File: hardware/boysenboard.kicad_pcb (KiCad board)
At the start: 4 copper layers, 68.6 x 53.3 mm, 97 parts, among them J1 1050171001, J2 54-00164, J3 NPTC101KFXC-RC, J4 NPTC081KFXC-RC, J5 Micro-SD, J6 NPTC081KFXC-RC, J7 NPTC061KFXC-RC, Q1 BSS308PEH6327XTSA1, SW1 PTS645SL70SMTR92LFS, U1 F1C200s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

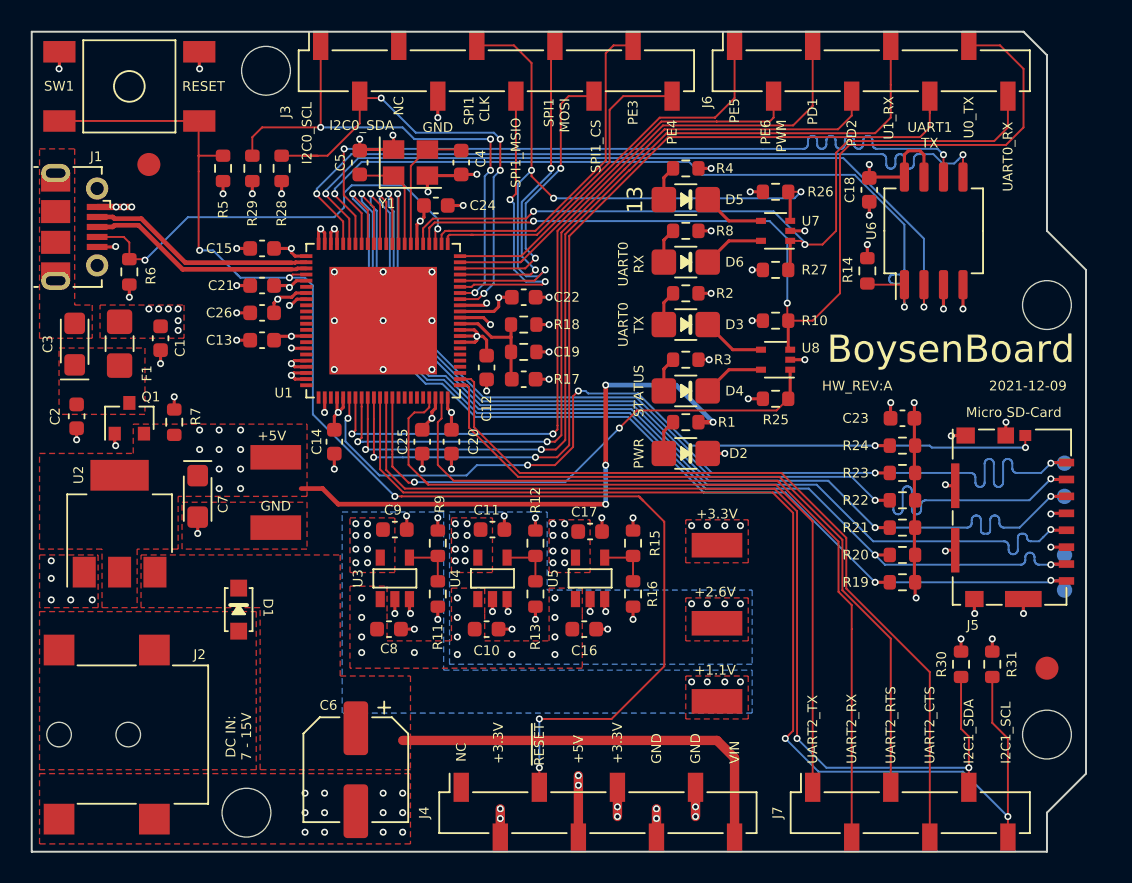
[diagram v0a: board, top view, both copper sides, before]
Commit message: Fixed footprint references and kicad 5->6 models
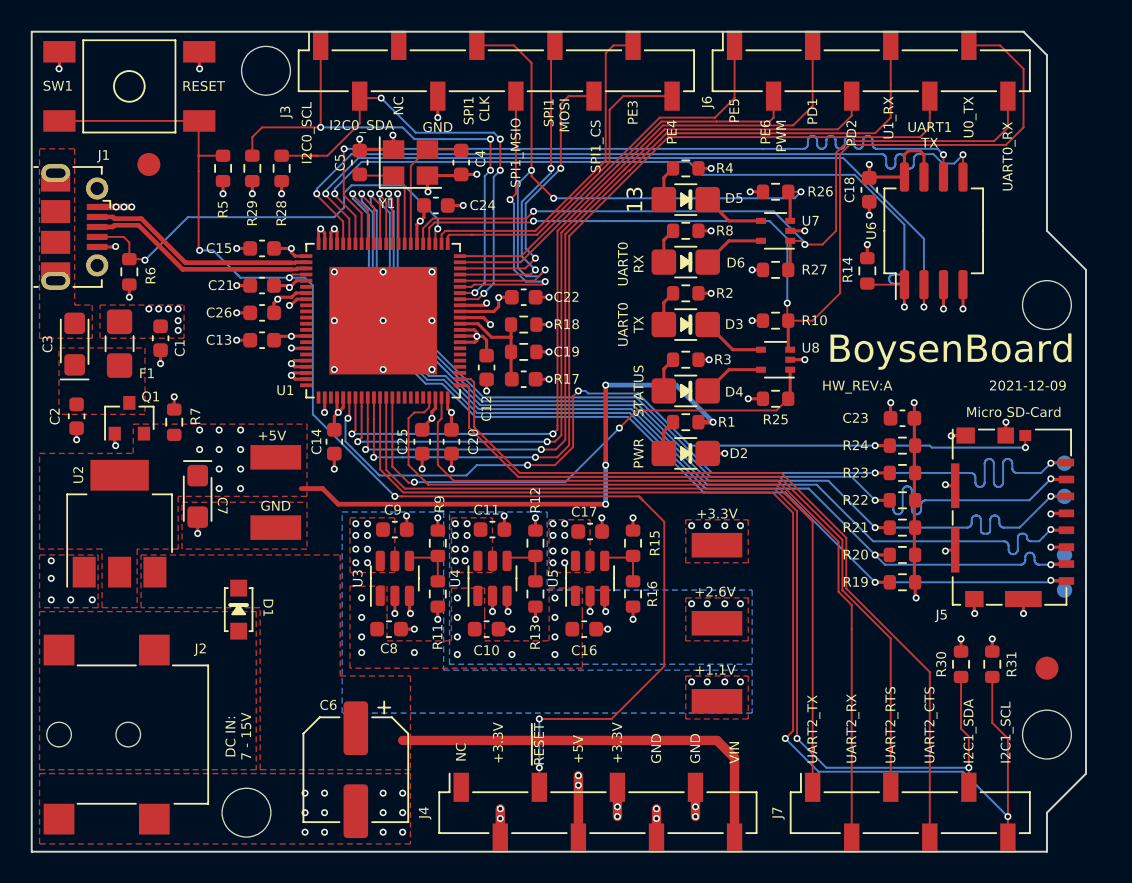
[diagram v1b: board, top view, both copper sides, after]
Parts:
- C3, C7: footprint licheeduino:CP_EIA-3216-18_Kemet-A -> boysenboard:CP_EIA-3216-18_Kemet-A
- D1: footprint licheeduino:D_SOD-123F -> boysenboard:D_SOD-123F
- D2, D3, D4, D5, D6: footprint licheeduino:LED_1206_3216Metric_Castellated -> boysenboard:LED_1206_3216Metric_Castellated
- F1: footprint licheeduino:Fuse_1206_3216Metric_Castellated -> boysenboard:Fuse_1206_3216Metric_Castellated
- H1, H2, H3, H4: footprint licheeduino:mounting_hole_125mil -> boysenboard:mounting_hole_125mil
- J1: footprint licheeduino:USB_Micro-B_Molex-105017-0001 -> boysenboard:USB_Micro-B_Molex-105017-0001
- J2: footprint licheeduino:barrel_jack_2.1mm -> boysenboard:barrel_jack_2.1mm
- J5: footprint licheeduino:micro-sd -> boysenboard:micro-sd
- SW1: footprint licheeduino:switch_tactile_6x6mm_smt -> boysenboard:switch_tactile_6x6mm_smt
- TP1, TP2, TP3, TP4, TP5: footprint licheeduino:test_point_RCSCTE -> boysenboard:test_point_RCSCTE
- U1: footprint licheeduino:QFN-88 -> boysenboard:QFN-88
- U3, U4, U5: footprint licheeduino:SOT-25 -> Package_TO_SOT_SMD:SOT-23-6

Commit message: Fixed PCB DRC violations caused by Kicad 5->6 conversion
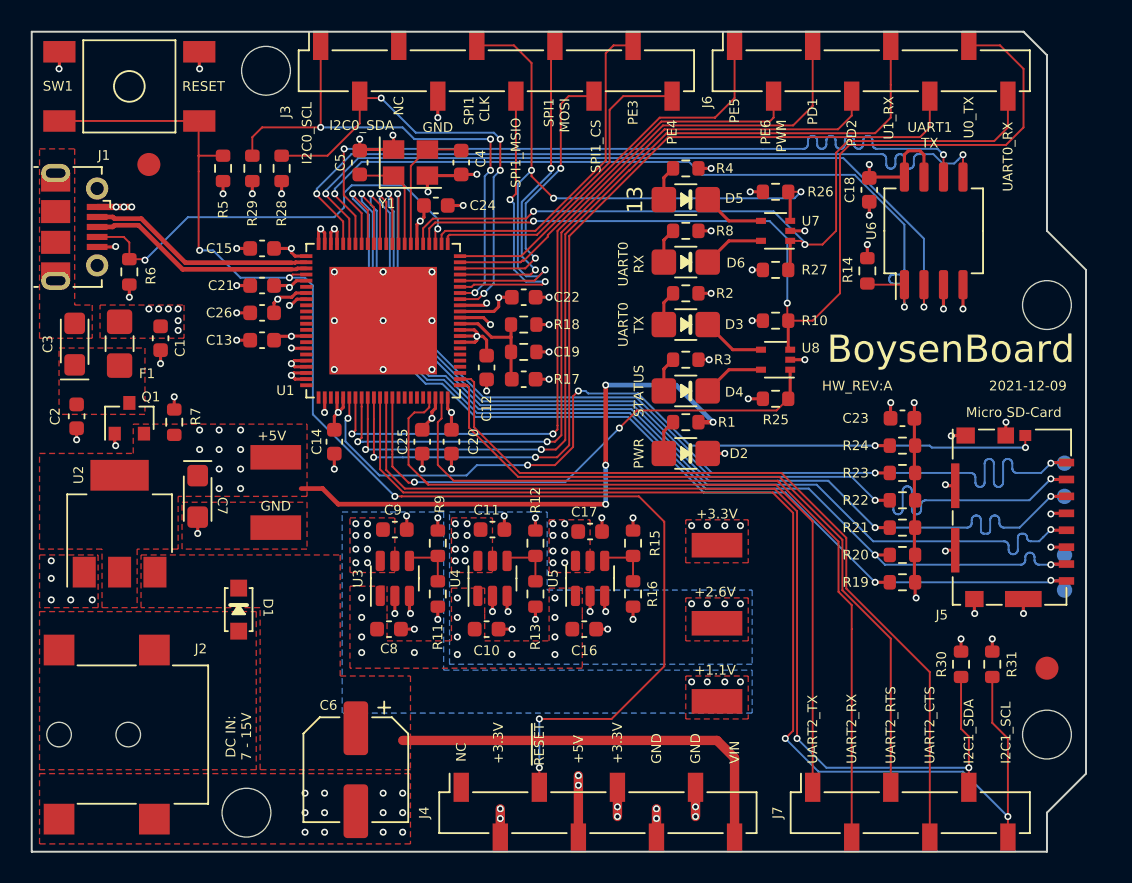
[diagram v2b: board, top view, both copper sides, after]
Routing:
- net /VIN: track 29.2 -> 27.3 mm
- net /PD4_UART1_TX: track 60.0 -> 59.0 mm
- net /I2C0_SDA: track 31.1 -> 30.2 mm
- net /~{RESET}: track 86.7 -> 86.2 mm
